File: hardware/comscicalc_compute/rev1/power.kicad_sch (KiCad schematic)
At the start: 44 parts, among them IC2 TPS92360DCKR, IC3 AP62300TWU-7, J3 USB4110-GF-A, SW2 SSSS211603, U1 USBLC6-2SC6

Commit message: Made yet another revision of the hardware using the rp2040
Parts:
- removed C11, C18: 100nF, Capacitor_SMD:C_0402_1005Metric, symbol Device:C_Small
- removed C15, C16, C17, C24, C27, C29: 22uF, Capacitor_SMD:C_0805_2012Metric, symbol Device:C_Small
- removed C19: 10uF, Capacitor_SMD:C_0805_2012Metric, symbol Device:C_Small
- removed C26, C28, C30: 10nF, Capacitor_SMD:C_0402_1005Metric, symbol Device:C_Small
- removed FB1: BLM21PG300SN1D, Resistor_SMD:R_0805_2012Metric, symbol Device:FerriteBead
- removed IC3: AP62300TWU-7, SOT95P280X100-6N, symbol SamacSys_Parts:AP62300TWU-7
- removed L2: 3.3uH, VLS5045EX-3R3N:IND_VLS5045EX-3R3N, symbol Device:L
- removed R16: 33.2k, Resistor_SMD:R_0402_1005Metric, symbol Device:R_Small
- removed R17: 10k, Resistor_SMD:R_0402_1005Metric, symbol Device:R_Small
- removed SW2: SSSS211603, SamacSys_Parts:SSSS211603, symbol Switch:SW_SPDT
- removed TP3, TP7: TestPoint, TestPoint:TestPoint_Pad_D1.5mm, symbol Connector:TestPoint
- added C39, C40: 22uF, Capacitor_SMD:C_0805_2012Metric, symbol Device:C_Small
- added R10, R7: 0R, Resistor_SMD:R_0402_1005Metric, symbol Device:R_Small
- added R11, R8: DNM, Resistor_SMD:R_0402_1005Metric, symbol Device:R_Small
- added R9: 10k, Resistor_SMD:R_0402_1005Metric, symbol Device:R_Small
- added SW2: JS202011JAQN, JS202011JAQN:JS202011JAQN, symbol JS202011JAQN:JS202011JAQN
- added U4: TPSM863253, RDX0007A-MFG, symbol ul_PTPSM863252RDXR:PTPSM863252RDXR
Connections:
- net +3V3: now also C39.1, C40.1, R10.2, R7.2, R9.2, U4.3 (VOUT); no longer C12.1, C13.1, C20.1, IC2.5 (VIN), L1.2
- net GND: now also C39.2, C40.2, R11.1, SW2.3, SW2.7, U4.4 (PGND)
- net PWR_EN: now also U4.6 (EN)
- net USB_CONN_D_N: now also U1.1 (I/O1); no longer U1.3 (I/O2)
- net USB_CONN_D_P: now also U1.3 (I/O2); no longer U1.1 (I/O1)
- net USB_D_N: now also FL1.4; no longer FL1.3
- net USB_D_P: now also FL1.3; no longer FL1.4
- net at C21.1, R20.1, R21.2: now also SW2.2, SW2.6
- net USB_POWER renamed +5V
- net +5V: now also C12.1, C13.1, R8.2, U4.1 (VIN)
- new net: R10.1, R11.2, U4.7 (FB)
- new net: R9.1, U4.5 (PG)
- new net 24V_IN: C20.1, IC2.5 (VIN), L1.2, R7.1, R8.1
- no-connect marks 3 -> 5
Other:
- note added: "Compatible with TPSM86325X"
- note added: "FB resistors TPSM86325[2,7]: R10 = 135k R11 = 30k FB resistors TPSM863253: R10 = 0R R11 = DNM"
- note added: "USB power filter - Needed?"
- note removed: "Bulk capacitance. To be spread out and placed near sinks."
- note removed: "Cheap 5V - 3V3, max 3A."
- note removed: "USB power filter"
- moved on the sheet: C12, C13, C21, R20, R21, TP1

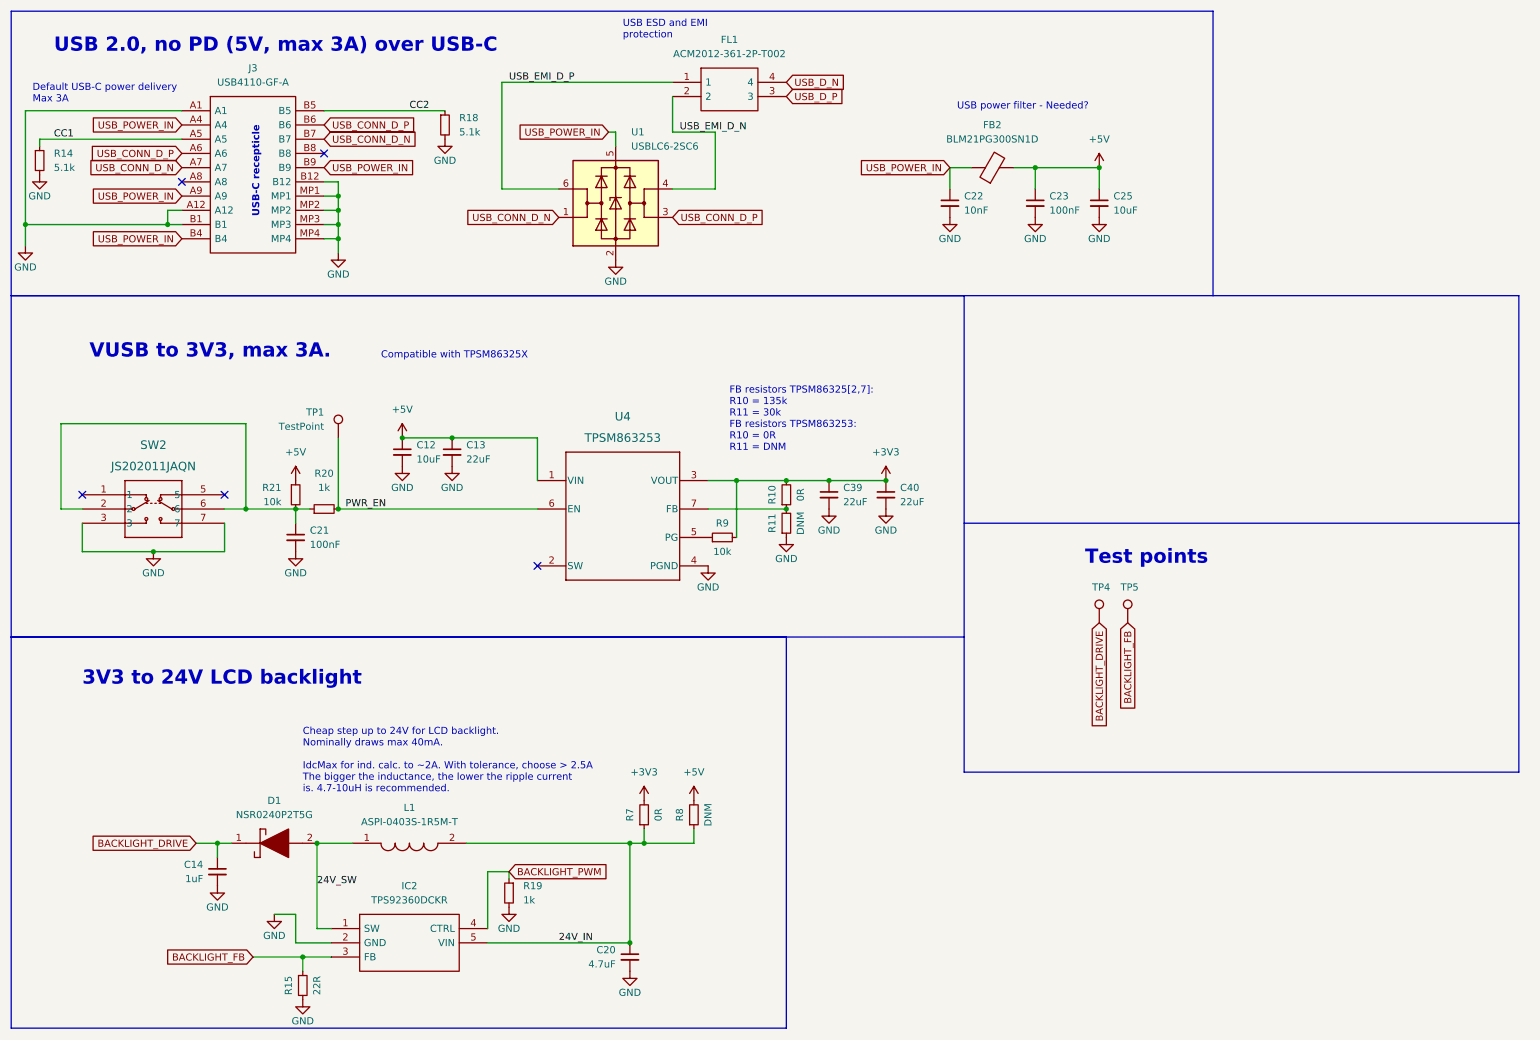
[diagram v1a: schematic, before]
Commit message: Added hardware changes and some of the missing fonts
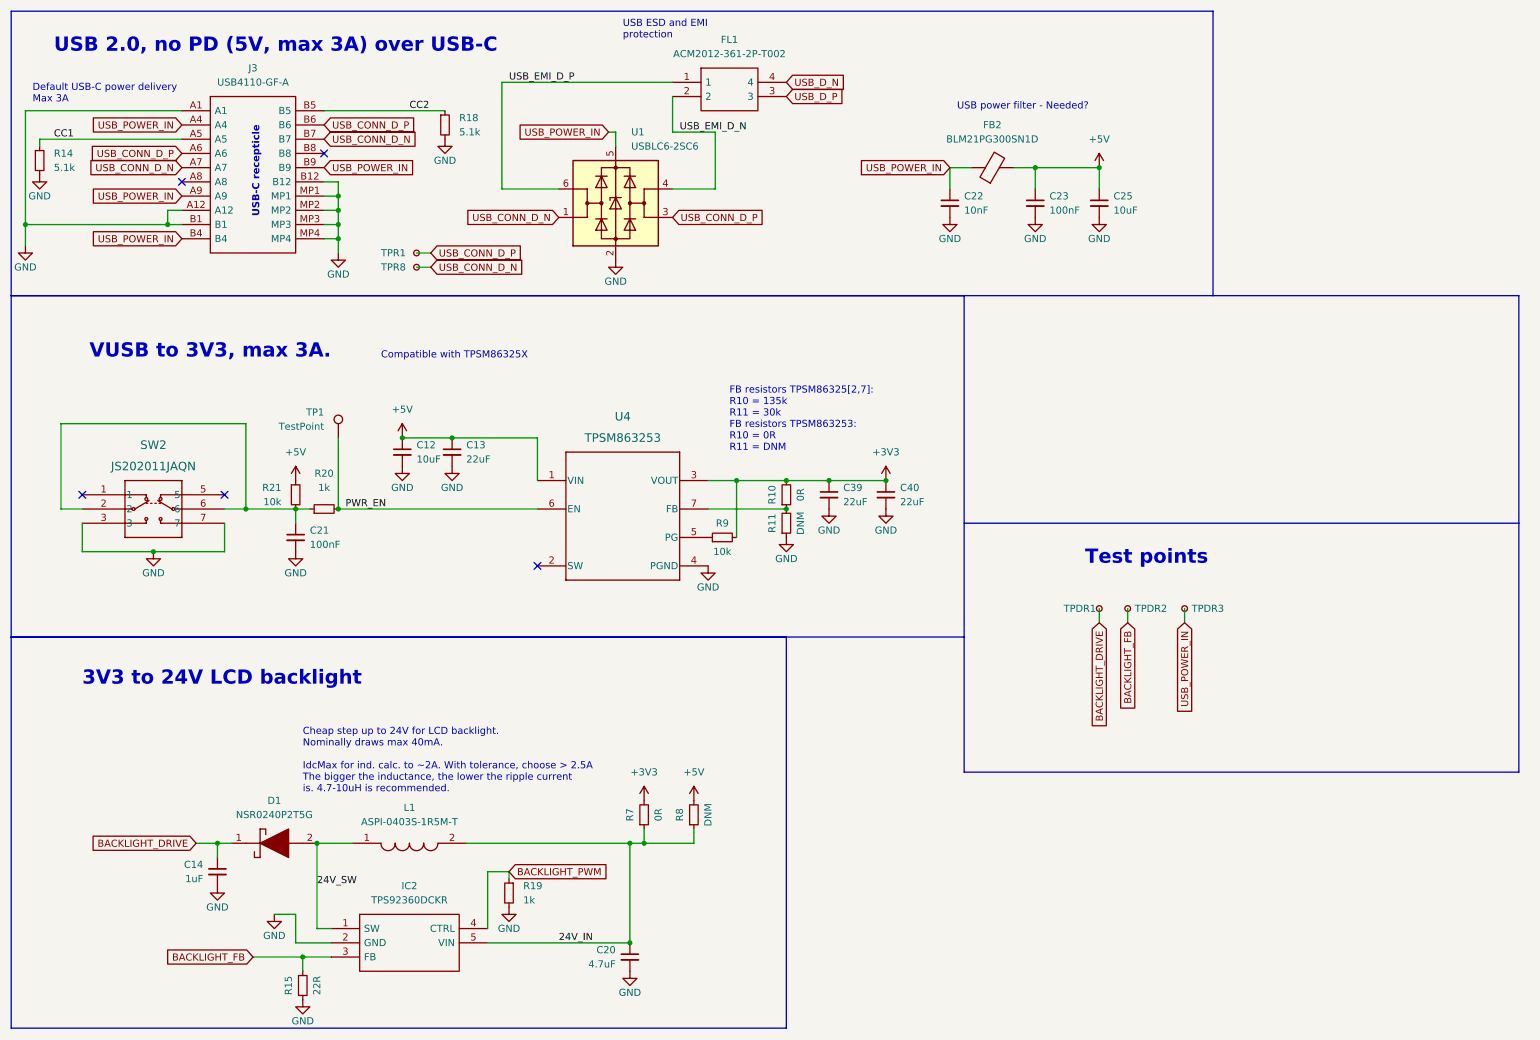
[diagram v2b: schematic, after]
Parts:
- removed TP4, TP5: TestPoint, TestPoint:TestPoint_Pad_D1.5mm, symbol Connector:TestPoint
- added TPDR1, TPDR2, TPDR3, TPR1, TPR8: TestPoint_Small, TestPoint:TestPoint_Pad_1.0x1.0mm, symbol Connector:TestPoint_Small
- TP1: footprint TestPoint:TestPoint_Pad_D1.5mm -> TestPoint:TestPoint_Pad_1.0x1.0mm
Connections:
- net BACKLIGHT_DRIVE: now also TPDR1.1
- net BACKLIGHT_FB: now also TPDR2.1
- net USB_CONN_D_N: now also TPR8.1
- net USB_CONN_D_P: now also TPR1.1
- net USB_POWER_IN: now also TPDR3.1
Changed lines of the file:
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@@
+    (stroke (width 0) (type default) (color 0 0 0 0))
+  )
+  (wire (pts (xy 215.9 121.92) (xy 215.9 124.46))
     (stroke (width 0) (type default) (color 0 0 0 0))
   )
@@
     (stroke (width 0) (type default) (color 0 0 0 0))
   )
+  (wire (pts (xy 210.82 121.92) (xy 210.82 124.46))
+    (stroke (width 0) (type default) (color 0 0 0 0))
+  )
   (wire (pts (xy 142.24 46.99) (xy 142.24 36.83))
     (stroke (width 0) (type default) (color 0 0 0 0))
@@
     (stroke (width 0) (type default) (color 0 0 0 0))
   )
+  (wire (pts (xy 91.44 58.42) (xy 88.9 58.42))
+    (stroke (width 0) (type default) (color 0 0 0 0))
+  )
   (wire (pts (xy 110.49 91.44) (xy 110.49 99.06))
     (stroke (width 0) (type default) (color 0 0 0 0))
@@
     (stroke (width 0) (type default) (color 0 0 0 0))
   )
+  (wire (pts (xy 91.44 60.96) (xy 88.9 60.96))
+    (stroke (width 0) (type default) (color 0 0 0 0))
+  )
   (polyline (pts (xy 16.51 196.85) (xy 16.51 127))
     (stroke (width 0) (type default) (color 0 0 0 0))
@@
   )
   (wire (pts (xy 58.42 104.14) (xy 58.42 88.9))
+    (stroke (width 0) (type default) (color 0 0 0 0))
+  )
+  (wire (pts (xy 226.06 121.92) (xy 226.06 124.46))
     (stroke (width 0) (type default) (color 0 0 0 0))
   )
@@
     )
   )
+  (global_label "USB_POWER_IN" (shape input) (at 226.06 124.46 270) (fields_autoplaced)
+    (effects (font (size 1.27 1.27)) (justify right))
+    (property "Intersheet References" "${INTERSHEET_REFS}" (id 0) (at 225.9806 141.0245 90)
+      (effects (font (size 1.27 1.27)) (justify right) hide)
+    )
+  )
   (global_label "USB_POWER_IN" (shape input) (at 46.99 35.56 180) (fields_autoplaced)
     (effects (font (size 1.27 1.27)) (justify right))
@@
     )
   )
+  (global_label "USB_CONN_D_P" (shape input) (at 91.44 58.42 0) (fields_autoplaced)
+    (effects (font (size 1.27 1.27)) (justify left))
+    (property "Intersheet References" "${INTERSHEET_REFS}" (id 0) (at 108.3674 58.4994 0)
+      (effects (font (size 1.27 1.27)) (justify left) hide)
+    )
+  )
   (global_label "USB_CONN_D_N" (shape input) (at 46.99 43.18 180) (fields_autoplaced)
     (effects (font (size 1.27 1.27)) (justify right))
@@
     )
   )
+  (global_label "USB_CONN_D_N" (shape input) (at 91.44 60.96 0) (fields_autoplaced)
+    (effects (font (size 1.27 1.27)) (justify left))
+    (property "Intersheet References" "${INTERSHEET_REFS}" (id 0) (at 108.4279 61.0394 0)
+      (effects (font (size 1.27 1.27)) (justify left) hide)
+    )
+  )
   (global_label "USB_CONN_D_P" (shape input) (at 46.99 40.64 180) (fields_autoplaced)
     (effects (font (size 1.27 1.27)) (justify right))
@@
     (pin "2")
   )
-  (symbol (lib_id "Connector:TestPoint") (at 210.82 124.46 0) (unit 1)
-    (in_bom yes) (on_board yes)
-    (property "Reference" "TP4" (id 0) (at 209.55 118.11 0)
-      (effects (font (size 1.27 1.27)) (justify left))
-    )
-    (property "Value" "TestPoint" (id 1) (at 207.01 118.11 0)
-      (effects (font (size 1.27 1.27)) (justify left) hide)
-    )
-    (property "Footprint" "TestPoint:TestPoint_Pad_D1.5mm" (id 2) (at 215.9 124.46 0)
-      (effects (font (size 1.27 1.27)) hide)
-    )
-    (property "Datasheet" "~" (id 3) (at 215.9 124.46 0)
+  (symbol (lib_id "Connector:TestPoint_Small") (at 226.06 121.92 0) (unit 1)
+    (in_bom yes) (on_board yes)
+    (property "Reference" "TPDR3" (id 0) (at 227.33 121.92 0)
+      (effects (font (size 1.27 1.27)) (justify left))
+    )
+    (property "Value" "TestPoint_Small" (id 1) (at 227.33 123.1899 0)
+      (effects (font (size 1.27 1.27)) (justify left) hide)
+    )
+    (property "Footprint" "TestPoint:TestPoint_Pad_1.0x1.0mm" (id 2) (at 231.14 121.92 0)
+      (effects (font (size 1.27 1.27)) hide)
+    )
+    (property "Datasheet" "~" (id 3) (at 231.14 121.92 0)
       (effects (font (size 1.27 1.27)) hide)
     )
@@
     (pin "2")
   )
+  (symbol (lib_id "Connector:TestPoint_Small") (at 88.9 60.96 0) (unit 1)
+    (in_bom yes) (on_board yes)
+    (property "Reference" "TPR8" (id 0) (at 82.55 60.96 0)
+      (effects (font (size 1.27 1.27)) (justify left))
+    )
+    (property "Value" "TestPoint_Small" (id 1) (at 90.17 62.2299 0)
+      (effects (font (size 1.27 1.27)) (justify left) hide)
+    )
+    (property "Footprint" "TestPoint:TestPoint_Pad_1.0x1.0mm" (id 2) (at 93.98 60.96 0)
+      (effects (font (size 1.27 1.27)) hide)
+    )
+    (property "Datasheet" "~" (id 3) (at 93.98 60.96 0)
+      (effects (font (size 1.27 1.27)) hide)
+    )
+    (pin "1")
+  )
   (symbol (lib_id "power:GND") (at 41.91 111.76 0) (unit 1)
     (in_bom yes) (on_board yes)
@@
     (pin "1")
     (pin "2")
-  )
-  (symbol (lib_id "Connector:TestPoint") (at 215.9 124.46 0) (unit 1)
-    (in_bom yes) (on_board yes)
-    (property "Reference" "TP5" (id 0) (at 214.63 118.11 0)
-      (effects (font (size 1.27 1.27)) (justify left))
-    )
-    (property "Value" "TestPoint" (id 1) (at 212.09 118.11 0)
-      (effects (font (size 1.27 1.27)) (justify left) hide)
-    )
-    (property "Footprint" "TestPoint:TestPoint_Pad_D1.5mm" (id 2) (at 220.98 124.46 0)
-      (effects (font (size 1.27 1.27)) hide)
-    )
-    (property "Datasheet" "~" (id 3) (at 220.98 124.46 0)
-      (effects (font (size 1.27 1.27)) hide)
-    )
-    (pin "1")
   )
   (symbol (lib_id "power:GND") (at 86.36 96.52 0) (unit 1)
@@
     (pin "5")
   )
+  (symbol (lib_id "Connector:TestPoint_Small") (at 210.82 121.92 0) (unit 1)
+    (in_bom yes) (on_board yes)
+    (property "Reference" "TPDR1" (id 0) (at 204.47 121.92 0)
+      (effects (font (size 1.27 1.27)) (justify left))
+    )
+    (property "Value" "TestPoint_Small" (id 1) (at 212.09 123.1899 0)
+      (effects (font (size 1.27 1.27)) (justify left) hide)
+    )
+    (property "Footprint" "TestPoint:TestPoint_Pad_1.0x1.0mm" (id 2) (at 215.9 121.92 0)
+      (effects (font (size 1.27 1.27)) hide)
+    )
+    (property "Datasheet" "~" (id 3) (at 215.9 121.92 0)
+      (effects (font (size 1.27 1.27)) hide)
+    )
+    (pin "1")
+  )
   (symbol (lib_id "power:GND") (at 127 186.69 0) (mirror y) (unit 1)
     (in_bom yes) (on_board yes)
@@
     (pin "1")
     (pin "2")
+  )
+  (symbol (lib_id "Connector:TestPoint_Small") (at 215.9 121.92 0) (unit 1)
+    (in_bom yes) (on_board yes)
+    (property "Reference" "TPDR2" (id 0) (at 217.17 121.92 0)
+      (effects (font (size 1.27 1.27)) (justify left))
+    )
+    (property "Value" "TestPoint_Small" (id 1) (at 217.17 123.1899 0)
+      (effects (font (size 1.27 1.27)) (justify left) hide)
+    )
+    (property "Footprint" "TestPoint:TestPoint_Pad_1.0x1.0mm" (id 2) (at 220.98 121.92 0)
+      (effects (font (size 1.27 1.27)) hide)
+    )
+    (property "Datasheet" "~" (id 3) (at 220.98 121.92 0)
+      (effects (font (size 1.27 1.27)) hide)
+    )
+    (pin "1")
   )
   (symbol (lib_id "power:GND") (at 95.25 96.52 0) (unit 1)
@@
     (pin "1")
   )
+  (symbol (lib_id "Connector:TestPoint_Small") (at 88.9 58.42 0) (unit 1)
+    (in_bom yes) (on_board yes)
+    (property "Reference" "TPR1" (id 0) (at 82.55 58.42 0)
+      (effects (font (size 1.27 1.27)) (justify left))
+    )
+    (property "Value" "TestPoint_Small" (id 1) (at 90.17 59.6899 0)
+      (effects (font (size 1.27 1.27)) (justify left) hide)
+    )
+    (property "Footprint" "TestPoint:TestPoint_Pad_1.0x1.0mm" (id 2) (at 93.98 58.42 0)
+      (effects (font (size 1.27 1.27)) hide)
+    )
+    (property "Datasheet" "~" (id 3) (at 93.98 58.42 0)
+      (effects (font (size 1.27 1.27)) hide)
+    )
+    (pin "1")
+  )
   (symbol (lib_id "power:+5V") (at 210.82 43.18 0) (unit 1)
     (in_bom yes) (on_board yes) (fields_autoplaced)
@@
       (effects (font (size 1.27 1.27)) (justify left))
     )
-    (property "Footprint" "TestPoint:TestPoint_Pad_D1.5mm" (id 2) (at 69.85 91.44 0)
-      (effects (font (size 1.27 1.27)) hide)
-    )
+    (property "Footprint" "TestPoint:TestPoint_Pad_1.0x1.0mm" (id 2) (at 69.85 91.44 0)
+      (effects (font (size 1.27 1.27)) hide)
+    )
